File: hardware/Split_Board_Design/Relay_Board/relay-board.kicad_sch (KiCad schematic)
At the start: 10 parts, among them J5 XT60PW-M, J6 Conn_01x06, J7 XT60PW-M

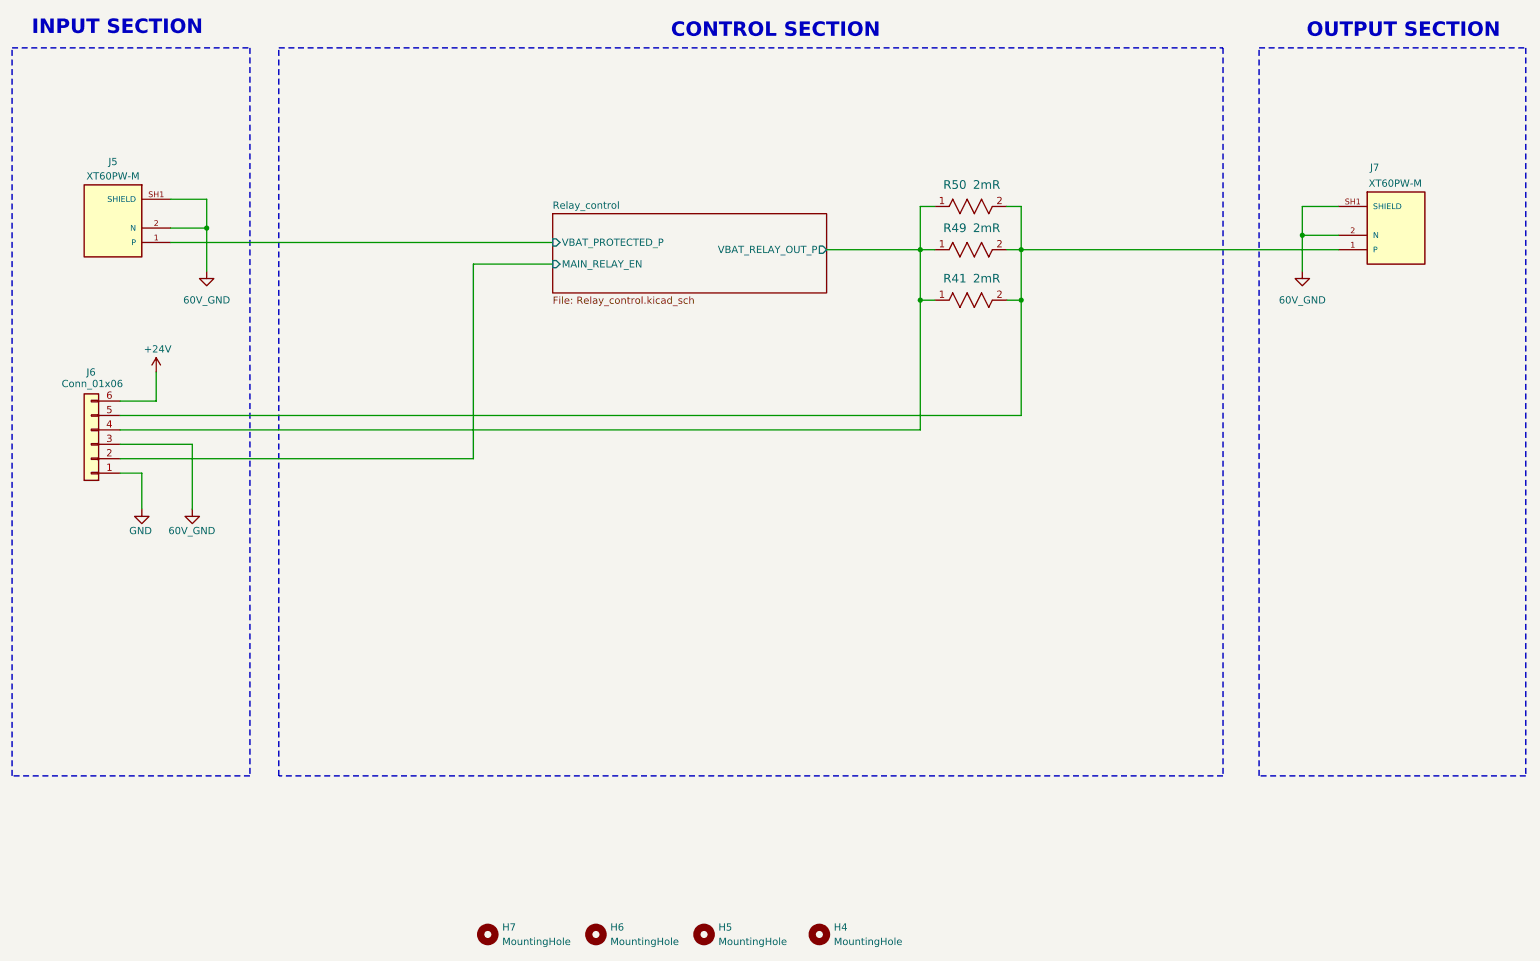
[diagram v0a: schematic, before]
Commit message: feat(layout): Finish demo layout of relay board
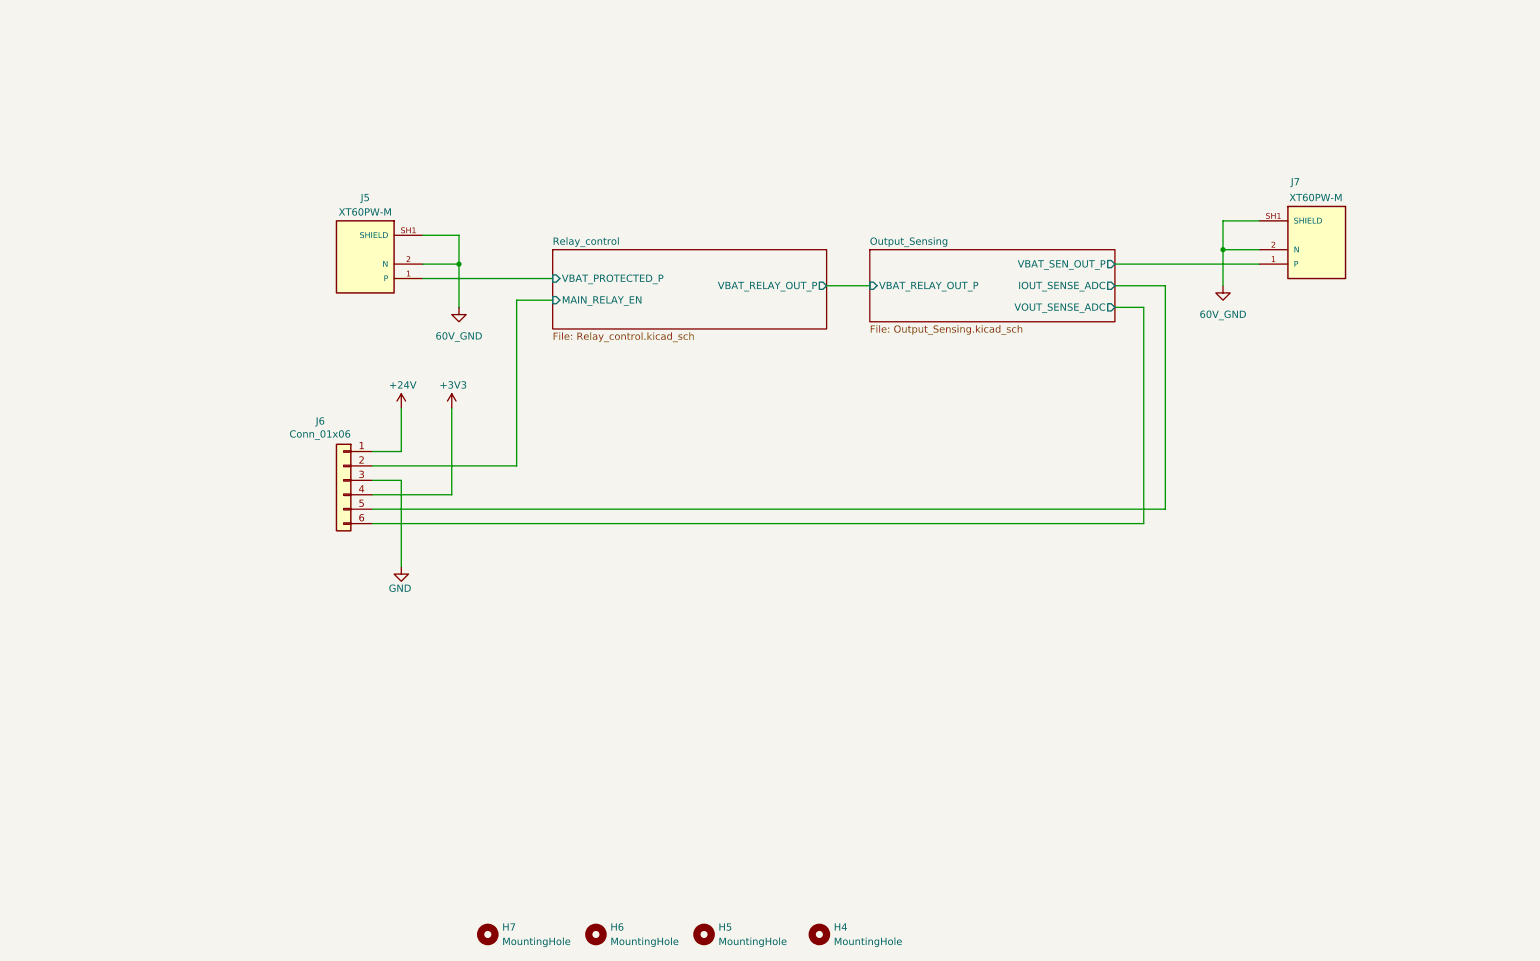
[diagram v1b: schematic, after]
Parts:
- removed R41, R49, R50: 2mR, RobotChargeController:RES_1L00x_BRN, symbol RobotChargeController:CSS2H-2512R-1L00F
- J6: Link to Buy (none) -> https://linhkien.cxtvn.com/3878-header-duc-xh254-6p-chan-co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
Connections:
- net +24V: now also J6.1 (Pin_1); no longer J6.6 (Pin_6)
- net 60V_GND: no longer J6.3 (Pin_3)
- net GND: now also J6.3 (Pin_3); no longer J6.1 (Pin_1)
- net Output_Sensing/IOUT_SENSE_ADC: now reaches J6.5 (Pin_5)
- net Output_Sensing/IOUT_SENSE_ADC: no longer J7.1 (P)
- net Relay_control/VBAT_RELAY_OUT_P renamed +3V3
- new net Output_Sensing/VBAT_SEN_OUT_P: J7.1 (P)
- new net Output_Sensing/VOUT_SENSE_ADC: J6.6 (Pin_6)
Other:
- added sheet Output_Sensing (Output_Sensing.kicad_sch)
- note removed: "CONTROL SECTION"
- note removed: "INPUT SECTION"
- note removed: "OUTPUT SECTION"
- moved on the sheet: J5, J6, J7

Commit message: feat(layout): update relay board layout
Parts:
- added J3: XT30PW-M, RobotChargeController:AMASS_XT30PW-M, symbol RobotChargeController:XT30PW-M
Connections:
- net +24V: now also J3.P; no longer J6.1 (Pin_1)
- net GND: now also J3.N; no longer J6.3 (Pin_3)
- no-connect marks 0 -> 2

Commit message: layout: update layout
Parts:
- removed J3: XT30PW-M, RobotChargeController:AMASS_XT30PW-M, symbol RobotChargeController:XT30PW-M
- added J11: Conn_01x02, Connector_Phoenix_MC:PhoenixContact_MC_1,5_2-G-3.81_1x02_P3.81mm_Horizontal, symbol Connector_Generic:Conn_01x02
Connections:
- net +24V: now also J11.2 (Pin_2)
- net GND: now also J6.1 (Pin_1), J6.3 (Pin_3), J11.1 (Pin_1)
- no-connect marks 2 -> 0
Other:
- moved on the sheet: J6
